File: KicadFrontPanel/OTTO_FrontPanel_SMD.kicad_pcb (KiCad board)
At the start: 2 copper layers, 297 x 95 mm, 62 parts, among them SW1 ALPS SKHC, SW10 ALPS SKHC, SW11 ALPS SKHC, SW12 ALPS SKHC, SW13 ALPS SKHC, SW14 ALPS SKHC, SW15 ALPS SKHC, SW16 ALPS SKHC, SW17 ALPS SKHC, SW18 ALPS SKHC, SW19 ALPS SKHC, SW2 ALPS SKHC, SW20 ALPS SKHC, SW21 ALPS SKHC, SW22 ALPS SKHC, SW23 ALPS SKHC, SW24 ALPS SKHC, SW25 ALPS SKHC, SW26 ALPS SKHC, SW27 6x6x13mm, SW28 6x6x13mm, SW29 6x6x13mm, SW3 ALPS SKHC, SW30 6x6x13mm, SW31 6x6x13mm, SW32 6x6x13mm, SW33 6x6x13mm, SW34 6x6x13mm, SW35 6x6x13mm, SW36 6x6x13mm, SW37 6x6x13mm, SW38 6x6x13mm, SW39 6x6x13mm, SW4 ALPS SKHC, SW40 6x6x13mm, SW41 6x6x13mm, SW42 6x6x13mm, SW43 6x6x13mm, SW44 6x6x13mm, SW45 6x6x13mm, SW46 6x6x13mm, SW47 6x6x13mm, SW5 ALPS SKHC, SW50 6x6x13mm, SW51 6x6x13mm, SW52 6x6x13mm, SW53 6x6x13mm, SW54 6x6x13mm, SW55 6x6x13mm, SW56 6x6x13mm, SW6 ALPS SKHC, SW7 ALPS SKHC, SW8 ALPS SKHC, SW9 ALPS SKHC

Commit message: Added front panel and shrunk board width
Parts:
- added REF**: AUX_BOARD, OTTO_Footprints_Lib:AUX_BOARD, F.Cu at (0.00, 120.0)
- added REF**: MAIN_BOARD, OTTO_Footprints_Lib:MAIN_BOARD, F.Cu at (0.00, 240.0)
- moved H204 25.1 mm to (-8.17, 15.7)
- moved H202 18.2 mm to (322.9, 95.5)
- moved H201 17.8 mm to (-0.75, 102.1)
- moved H205 17.0 mm to (322.4, 13.0)
- moved SW27 4.50 mm to (221.7, 59.9)
- moved SW28 4.50 mm to (233.7, 59.9)
- moved SW29 4.50 mm to (245.7, 59.9)
- moved SW30 4.50 mm to (257.7, 59.9)
- moved SW31 4.50 mm to (269.7, 59.9)
- moved SW32 4.50 mm to (287.7, 59.9)
- moved SW33 4.50 mm to (299.7, 59.9)
- moved SW34 4.50 mm to (221.7, 47.9)
- moved SW35 4.50 mm to (233.7, 47.9)
- moved SW36 4.50 mm to (245.7, 47.9)
- moved SW37 4.50 mm to (257.7, 47.9)
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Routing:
- added copper zone on B.Cu, net (none)
- added copper zone on F.Cu, net (none)
- removed copper zone on B.Cu, net +5V_LEDS
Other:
- board size 297 x 95 mm -> 291.5 x 98.4 mm

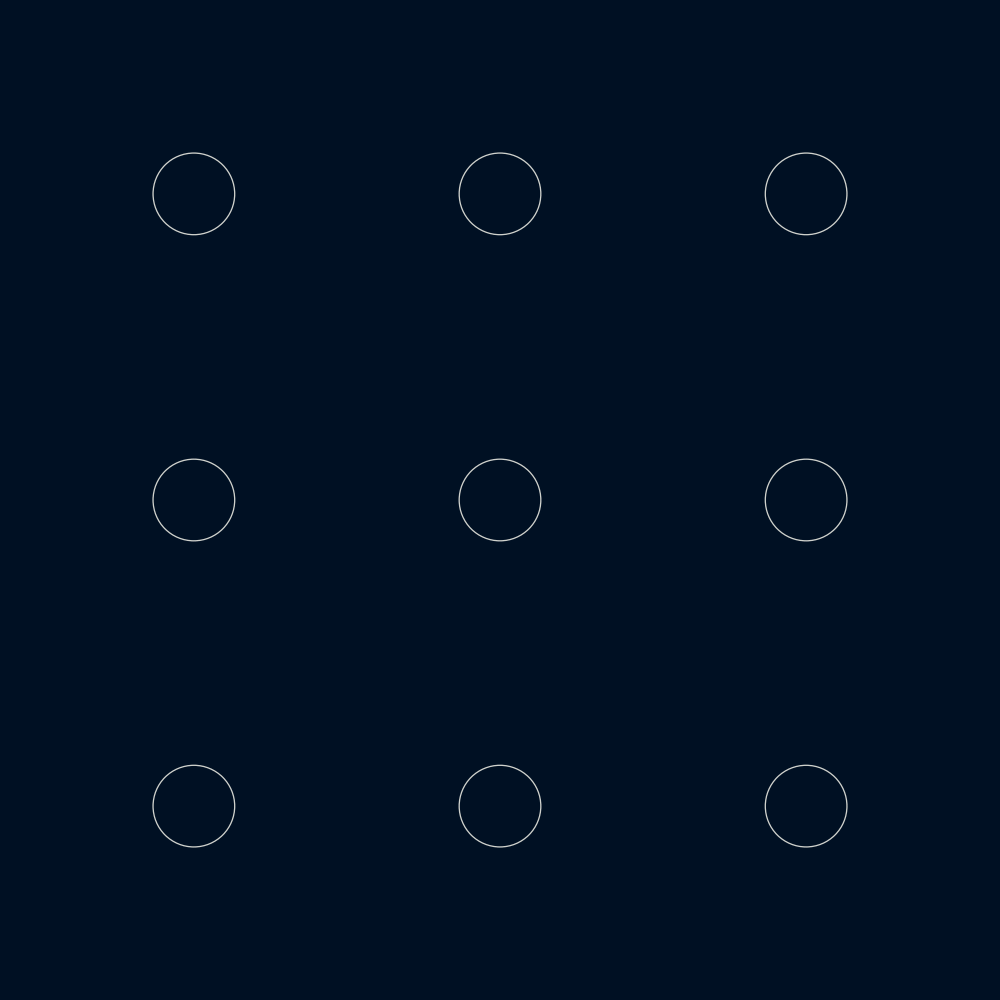
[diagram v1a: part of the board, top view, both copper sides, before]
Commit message: Inserted icons
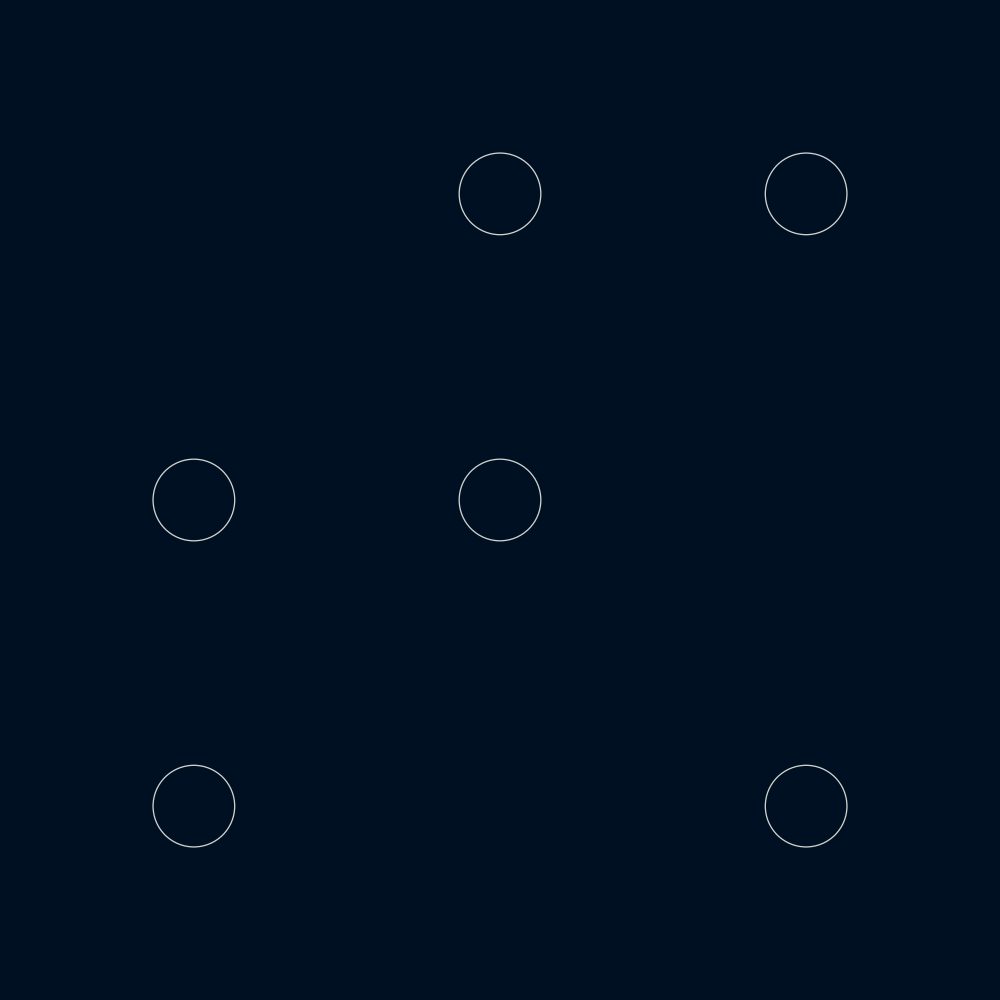
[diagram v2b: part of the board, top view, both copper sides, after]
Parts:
- removed SW27, SW28, SW29, SW30, SW31, SW34, SW35, SW36, SW37, SW39, SW40, SW41, SW42, SW43, SW44, SW45, SW46, SW47, SW50, SW51, SW52, SW53, SW54, SW55, SW56: 6x6x13mm, OTTO_Footprints_Lib:6x6mm_Switch
- added G***: LOGO, OTTO_Icons_Lib:f_icon, F.Cu at (269.7, 59.9)
- added G***: LOGO, OTTO_Icons_Lib:record, F.Cu at (287.7, 35.9)
- added G***: LOGO, OTTO_Icons_Lib:master, F.Cu at (299.7, 23.9)
- added G***: LOGO, OTTO_Icons_Lib:settings, F.Cu at (287.7, 23.9)
- added G***: LOGO, OTTO_Icons_Lib:shift, F.Cu at (221.7, 59.9)
- added G***: LOGO, OTTO_Icons_Lib:linein, F.Cu at (221.7, 47.9)
- added G***: LOGO, OTTO_Icons_Lib:fx2, F.Cu at (269.7, 35.9)
- added G***: LOGO, OTTO_Icons_Lib:sends, F.Cu at (257.7, 35.9)
- added G***: LOGO, OTTO_Icons_Lib:sequencer, F.Cu at (233.7, 35.9)
- added G***: LOGO, OTTO_Icons_Lib:routing, F.Cu at (221.7, 35.9)
- added G***: LOGO, OTTO_Icons_Lib:fx1, F.Cu at (269.7, 23.9)
- added G***: LOGO, OTTO_Icons_Lib:e_icon, F.Cu at (257.7, 59.9)
- added G***: LOGO, OTTO_Icons_Lib:adsr-test, F.Cu at (257.7, 23.9)
- added G***: LOGO, OTTO_Icons_Lib:synth, F.Cu at (245.7, 23.9)
- added G***: LOGO, OTTO_Icons_Lib:arpeggiator, F.Cu at (233.7, 23.9)
- added G***: LOGO, OTTO_Icons_Lib:d_icon, F.Cu at (245.7, 59.9)
- added G***: LOGO, OTTO_Icons_Lib:c_icon, F.Cu at (233.7, 59.9)
- added G***: LOGO, OTTO_Icons_Lib:b_icon, F.Cu at (257.7, 47.9)
- added G***: LOGO, OTTO_Icons_Lib:a_icon, F.Cu at (245.7, 47.9)
- added G***: LOGO, OTTO_Icons_Lib:plus, F.Cu at (299.7, 47.9)
- added G***: LOGO, OTTO_Icons_Lib:minus, F.Cu at (287.7, 47.9)
- added G***: LOGO, OTTO_Icons_Lib:play, F.Cu at (299.7, 35.9)

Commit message: add voices
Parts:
- added G***: LOGO, OTTO_Icons_Lib:voices, F.Cu at (221.7, 23.9)
- added G***: LOGO, OTTO_Icons_Lib:sampler-v2, F.Cu at (245.7, 35.9)
- added G***: LOGO, OTTO_Icons_Lib:looper-v2, F.Cu at (233.7, 47.9)

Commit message: Inserted button grid on front plate
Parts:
- added G***: LOGO, OTTO_Icons_Lib:icons_grid, F.Cu at (256.4, 37.5)
- G***: footprint OTTO_Icons_Lib:shift -> OTTO_Icons_Lib:only_hole
- G***: footprint OTTO_Icons_Lib:sampler-v2 -> OTTO_Icons_Lib:only_hole
- G***: footprint OTTO_Icons_Lib:sequencer -> OTTO_Icons_Lib:only_hole
- G***: footprint OTTO_Icons_Lib:routing -> OTTO_Icons_Lib:only_hole
- G***: footprint OTTO_Icons_Lib:master -> OTTO_Icons_Lib:only_hole
- G***: footprint OTTO_Icons_Lib:settings -> OTTO_Icons_Lib:only_hole
- G***: footprint OTTO_Icons_Lib:fx1 -> OTTO_Icons_Lib:only_hole
- G***: footprint OTTO_Icons_Lib:adsr-test -> OTTO_Icons_Lib:only_hole
- G***: footprint OTTO_Icons_Lib:synth -> OTTO_Icons_Lib:only_hole
- G***: footprint OTTO_Icons_Lib:arpeggiator -> OTTO_Icons_Lib:only_hole
- G***: footprint OTTO_Icons_Lib:voices -> OTTO_Icons_Lib:only_hole
- G***: footprint OTTO_Icons_Lib:plus -> OTTO_Icons_Lib:only_hole
- G***: footprint OTTO_Icons_Lib:minus -> OTTO_Icons_Lib:only_hole
- G***: footprint OTTO_Icons_Lib:looper-v2 -> OTTO_Icons_Lib:only_hole
- G***: footprint OTTO_Icons_Lib:linein -> OTTO_Icons_Lib:only_hole
- G***: footprint OTTO_Icons_Lib:play -> OTTO_Icons_Lib:only_hole
- G***: footprint OTTO_Icons_Lib:record -> OTTO_Icons_Lib:only_hole
- G***: footprint OTTO_Icons_Lib:fx2 -> OTTO_Icons_Lib:only_hole
- G***: footprint OTTO_Icons_Lib:sends -> OTTO_Icons_Lib:only_hole

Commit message: Add HEX spacers and fix AUX LED pinouts
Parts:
- moved REF** 240.0 mm to (0.00, 0.00)
- moved REF** 120.0 mm to (0.00, 0.00)
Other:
- outline, holes or cut-outs redrawn
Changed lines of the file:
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@@
-(kicad_pcb (version 20171130) (host pcbnew 5.1.5+dfsg1-2build2)
+(kicad_pcb (version 20171130) (host pcbnew 5.1.6)
   (general
     (thickness 1.2)
@@
     (solder_mask_min_width 0.12)
     (aux_axis_origin 40.5 196.5)
-    (grid_origin 233.7 23.85)
     (visible_elements 7EFFFE7F)
     (pcbplotparams
@@
   )
   (module OTTO_Footprints_Lib:AUX_BOARD (layer F.Cu)
-    (at 0 120)
+    (at 0 0)
     (fp_text reference REF** (at 0 0.5) (layer F.SilkS)
       (effects (font (size 1 1) (thickness 0.15)))
@@
     (fp_circle (center 0 0) (end 0 4) (layer F.SilkS) (width 0.12))
     (model ${KIPRJMOD}/../KicadAUXBoard/OTTO_AUX_SMD.wrl
-      (offset (xyz 0 0 -4.35))
+      (offset (xyz 0 0 -4.8))
       (scale (xyz 1 1 1))
       (rotate (xyz 0 0 0))
@@
   )
   (module OTTO_Footprints_Lib:MAIN_BOARD (layer F.Cu)
-    (at 0 240)
+    (at 0 0)
     (fp_text reference REF** (at 0 0.5) (layer F.SilkS)
       (effects (font (size 1 1) (thickness 0.15)))
@@
     (fp_circle (center 0 0) (end 0 5) (layer F.SilkS) (width 0.12))
     (model ${KIPRJMOD}/../KiCad/OTTOdiy_SMD.wrl
-      (offset (xyz 0 0 -11.95))
+      (offset (xyz 0 0 -12.4))
       (scale (xyz 1 1 1))
       (rotate (xyz 0 0 0))
@@
   (gr_arc (start 306.47 106.3) (end 306.47 106.8) (angle -90) (layer Edge.Cuts) (width 0.15))
   (gr_arc (start 306.47 8.9) (end 306.97 8.9) (angle -90) (layer Edge.Cuts) (width 0.15))
-  (target plus (at 0 0) (size 5) (width 0.15) (layer Edge.Cuts))
-  (gr_arc (start 199.29 60.95) (end 199.29 61.7) (angle -90) (layer Edge.Cuts) (width 0.15))
-  (gr_arc (start 143.191041 60.95) (end 142.441041 60.95) (angle -90) (layer Edge.Cuts) (width 0.15))
+  (target plus (at 0 145) (size 5) (width 0.15) (layer Edge.Cuts))
+  (gr_arc (start 199.34 60.7) (end 199.34 61.45) (angle -90) (layer Edge.Cuts) (width 0.15))
+  (gr_arc (start 143.241041 60.7) (end 142.491041 60.7) (angle -90) (layer Edge.Cuts) (width 0.15))
   (gr_line (start 23.7 85.5) (end 28.7 85.5) (layer F.SilkS) (width 1))
   (gr_line (start 26.8423 14.676691) (end 26.83632 14.6481) (layer Dwgs.User) (width 0.2))
@@
   )
   (gr_line (start 306.47 8.4) (end 15.93 8.4) (layer Edge.Cuts) (width 0.15))
-  (gr_arc (start 143.19 19.25) (end 143.19 18.5) (angle -90) (layer Edge.Cuts) (width 0.15))
-  (gr_arc (start 199.29 19.25) (end 200.04 19.25) (angle -90) (layer Edge.Cuts) (width 0.15))
-  (gr_line (start 143.19 18.5) (end 199.29 18.5) (layer Edge.Cuts) (width 0.15))
-  (gr_line (start 143.191041 61.7) (end 199.29 61.7) (layer Edge.Cuts) (width 0.15))
-  (gr_line (start 142.44 19.25) (end 142.441041 60.95) (layer Edge.Cuts) (width 0.15))
-  (gr_line (start 200.04 19.25) (end 200.04 60.95) (layer Edge.Cuts) (width 0.15))
+  (gr_arc (start 143.24 19) (end 143.24 18.25) (angle -90) (layer Edge.Cuts) (width 0.15))
+  (gr_arc (start 199.34 19) (end 200.09 19) (angle -90) (layer Edge.Cuts) (width 0.15))
+  (gr_line (start 143.24 18.25) (end 199.34 18.25) (layer Edge.Cuts) (width 0.15))
+  (gr_line (start 143.241041 61.45) (end 199.34 61.45) (layer Edge.Cuts) (width 0.15))
+  (gr_line (start 142.49 19) (end 142.491041 60.7) (layer Edge.Cuts) (width 0.15))
+  (gr_line (start 200.09 19) (end 200.09 60.7) (layer Edge.Cuts) (width 0.15))
   (target plus (at 0 114.3) (size 5) (width 0.15) (layer Edge.Cuts))
   (target plus (at 330.2 0) (size 5) (width 0.15) (layer Edge.Cuts))

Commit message: Revert "Add bracket step files"
This reverts commit c21e747328c344bdd5d7dfb352835a19e2e00d67.
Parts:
- added ?: MountingHole_2.7mm_M2.5, MountingHole:MountingHole_2.7mm_M2.5, F.Cu at (161.2, 80.6)
- added REF**: RightAngle_Small, OTTO_Footprints_Lib:RightAngle_Small, B.Cu at (35.0, 109.6)
- added REF**: RightAngle_Small, OTTO_Footprints_Lib:RightAngle_Small, B.Cu at (106.9, 109.6)
- added REF**: RightAngle_Small, OTTO_Footprints_Lib:RightAngle_Small, B.Cu at (209.4, 9.32)
- added REF**: RightAngle_Small, OTTO_Footprints_Lib:RightAngle_Small, B.Cu at (289.6, 9.32)
- added REF**: RightAngle_Large, OTTO_Footprints_Lib:RightAngle_Large, B.Cu at (50.6, 9.32)
- added REF**: RightAngle_Small, OTTO_Footprints_Lib:RightAngle_Small, B.Cu at (215.4, 109.6)
- added REF**: RightAngle_Small, OTTO_Footprints_Lib:RightAngle_Small, B.Cu at (287.4, 109.6)
- added REF**: RightAngle_Large, OTTO_Footprints_Lib:RightAngle_Large, B.Cu at (114.0, 9.32)
- G***: footprint OTTO_Icons_Lib:icons_grid -> OTTO_Icons_Lib:icons_grid_v2
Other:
- board size 291.5 x 98.4 mm -> 294.5 x 102.3 mm

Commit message: Before 2 designs
Fix paths for brackets.
Before splitting into 2 designs for beta test.
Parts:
- added G***: LOGO, OTTO_Icons_Lib:logo, F.Cu at (33.6, 25.7)
- G***: footprint OTTO_Icons_Lib:icons_grid_v2 -> OTTO_Icons_Lib:icons_grid_v3
- moved G*** 0.36 mm to (256.1, 37.6)

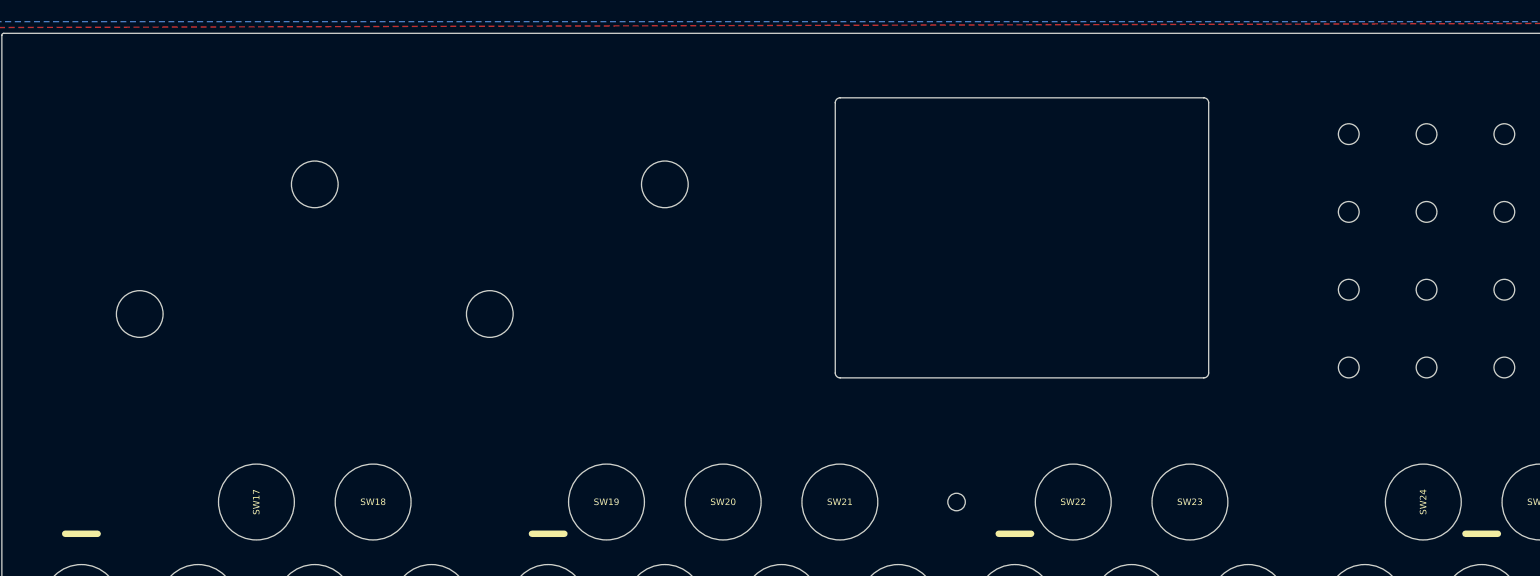
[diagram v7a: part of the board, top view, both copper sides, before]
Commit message: Split to 2 frontplates
Duplicated frontplate project
Finished non-copper version
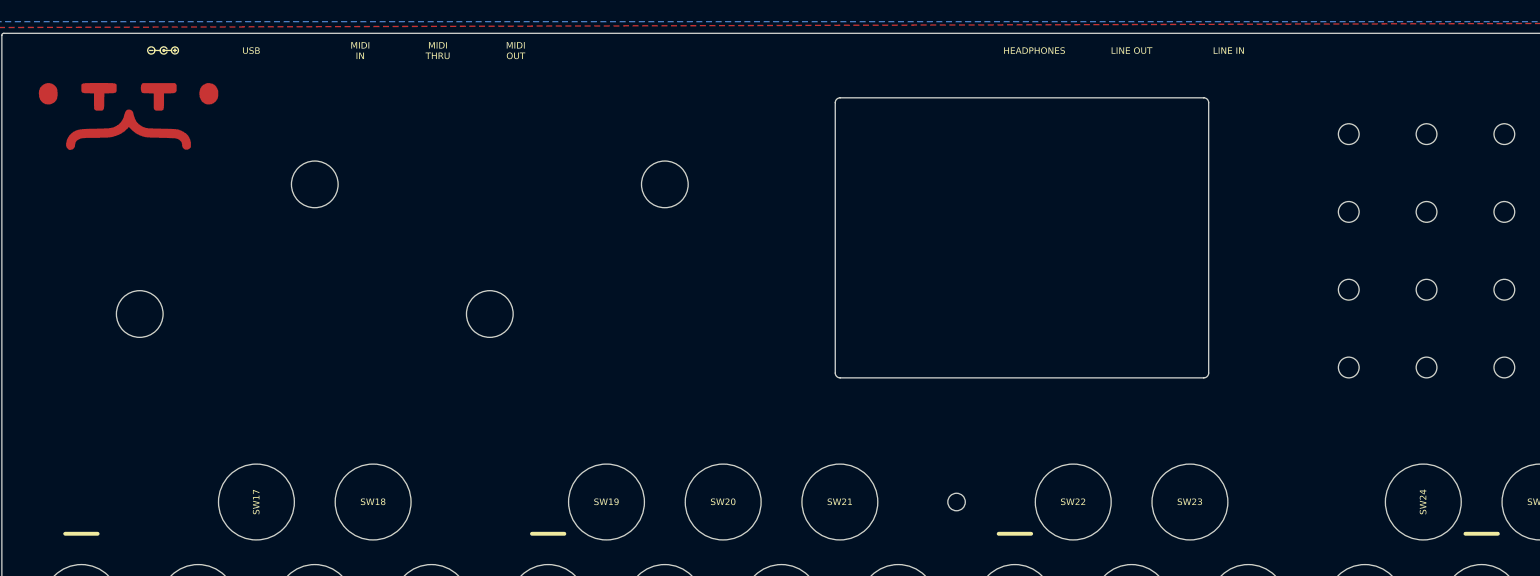
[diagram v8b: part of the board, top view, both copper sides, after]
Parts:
- G***: footprint OTTO_Icons_Lib:icons_grid_v3 -> OTTO_Icons_Lib:icons_grid_v3_circularBmask
- moved G*** 5.03 mm to (33.5, 20.7)
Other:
- board text added: "HEADPHONES"
- board text added: "LINE IN"
- board text added: "LINE OUT"
- board text added: "MIDI IN"
- board text added: "MIDI OUT"
- board text added: "MIDI THRU"
- board text added: "USB"
